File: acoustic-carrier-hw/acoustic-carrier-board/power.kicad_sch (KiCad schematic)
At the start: 59 parts, among them IC1 ECP5-BGA256, U6 TLV62569DRL, U7 TLV62569DRL, U8 TLV62569DRL

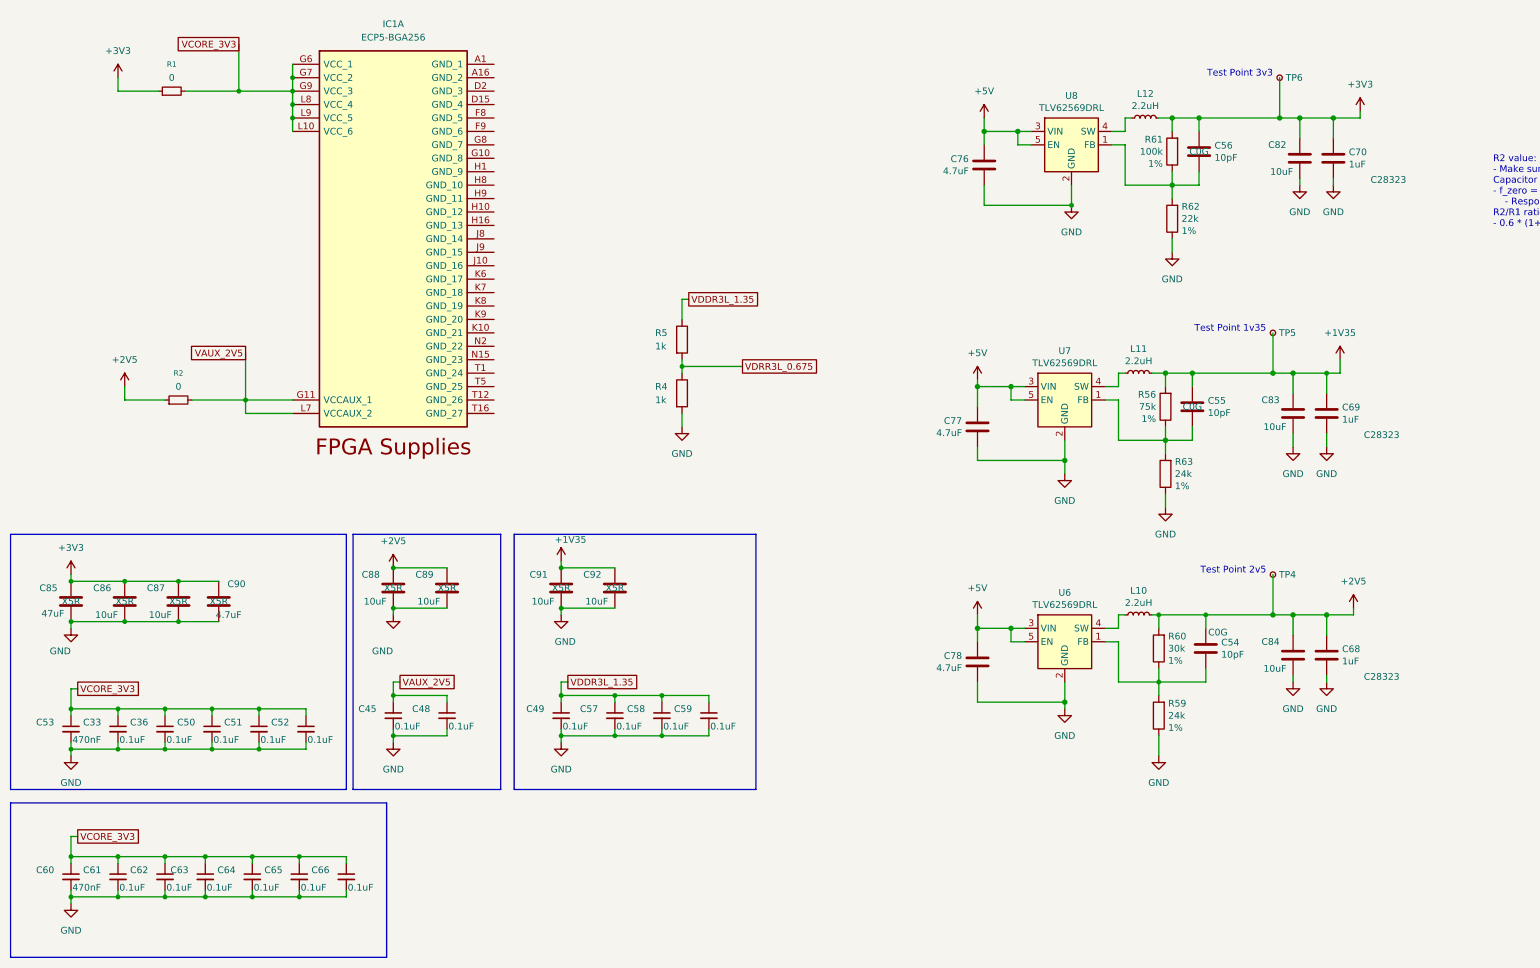
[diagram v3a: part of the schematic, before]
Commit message: [carrier] Added space for ferrite bead in between bulk and decoupling caps
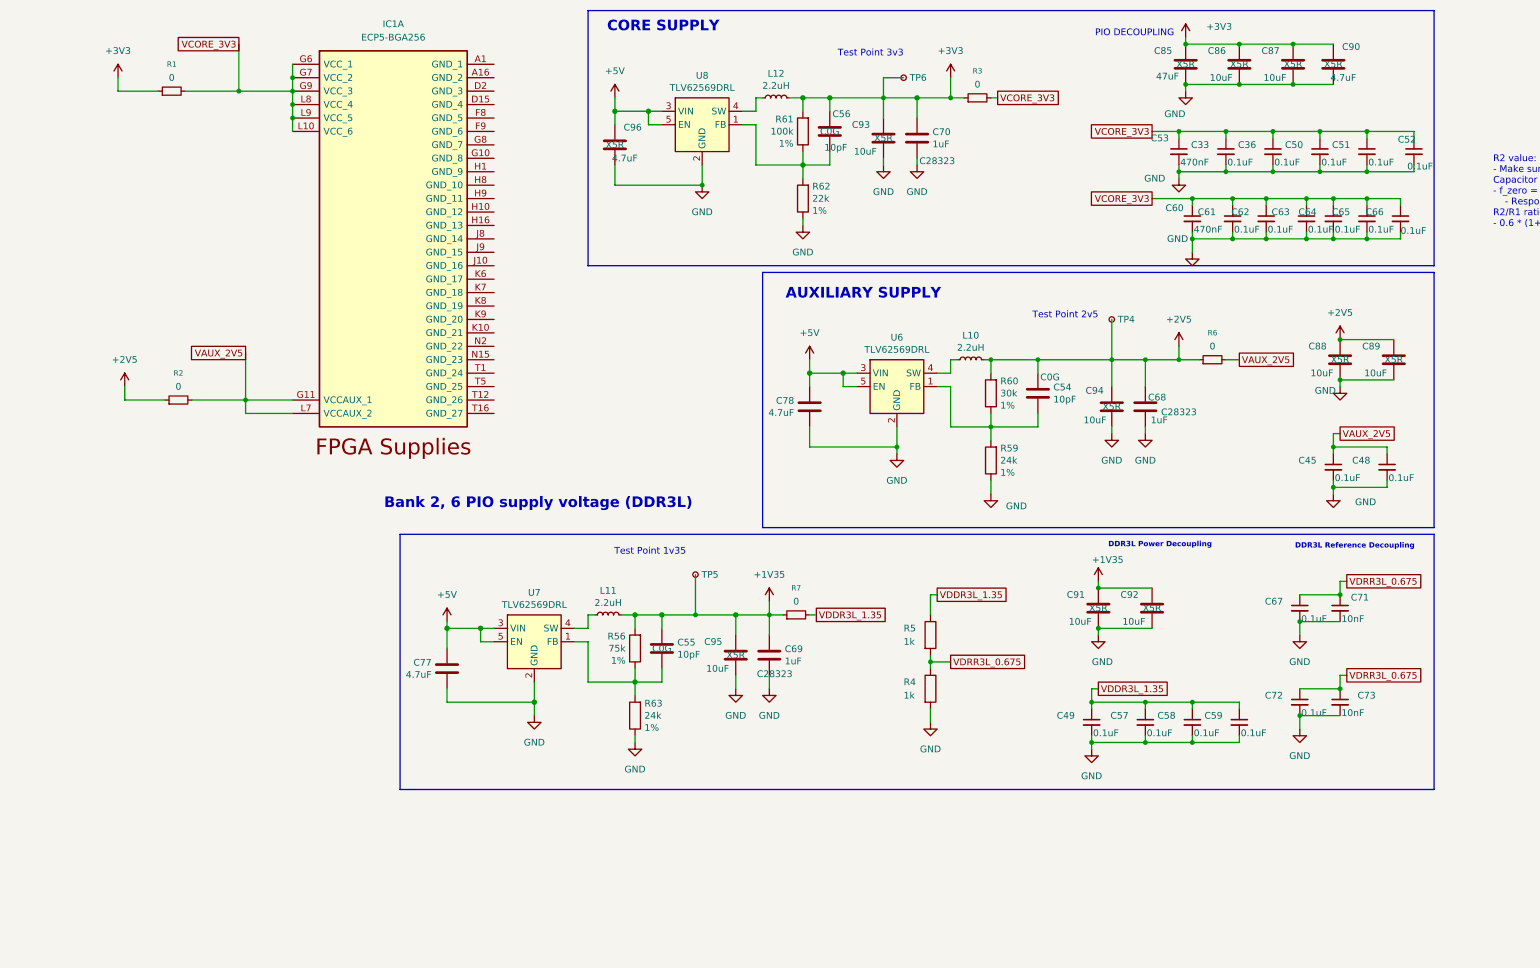
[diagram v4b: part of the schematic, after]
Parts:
- removed C76: 4.7uF, Capacitor_SMD:C_0402_1005Metric, symbol Device:C
- removed C82, C83, C84: 10uF, Capacitor_SMD:C_0603_1608Metric, symbol Device:C
- added C67, C72: 0.1uF, Capacitor_SMD:C_0402_1005Metric, symbol Device:C_Small
- added C71, C73: 10nF, Capacitor_SMD:C_0402_1005Metric, symbol Device:C_Small
- added C93, C94, C95: 10uF, Capacitor_SMD:C_0603_1608Metric, symbol Device:C
- added C96: 4.7uF, Capacitor_SMD:C_0402_1005Metric, symbol Device:C
- added R3, R6, R7: 0, Resistor_SMD:R_0805_2012Metric_Pad1.20x1.40mm_HandSolder, symbol Device:R_Small
- TP6: footprint TestPoint:TestPoint_Pad_D1.5mm -> (none); LPN (none) -> DNP; PN DNP -> (none)
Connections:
- net +1V35: now also C95.1, R7.1
- net +2V5: now also C94.1, R6.1
- net +3V3: now also C93.1, R3.1
- net +5V: now also C96.1
- net GND: now also C67.2, C71.2, C72.2, C73.2, C93.2, C94.2, C95.2, C96.2
- net VAUX_2V5: now also R6.2
- net VCORE_3V3: now also R3.2
- net VDDR3L_1.35: now also R7.2
- net VDRR3L_0.675: now also C67.1, C71.1, C72.1, C73.1
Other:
- note added: "AUXILIARY SUPPLY"
- note added: "Bank 2, 6 PIO supply voltage (DDR3L)"
- note added: "CORE SUPPLY"
- note added: "DDR3L Power Decoupling"
- note added: "DDR3L Reference Decoupling"
- note added: "PIO DECOUPLING"
- moved on the sheet: C33, C36, C45, C48, C49, C50, C51, C52, C53, C54, C55, C56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

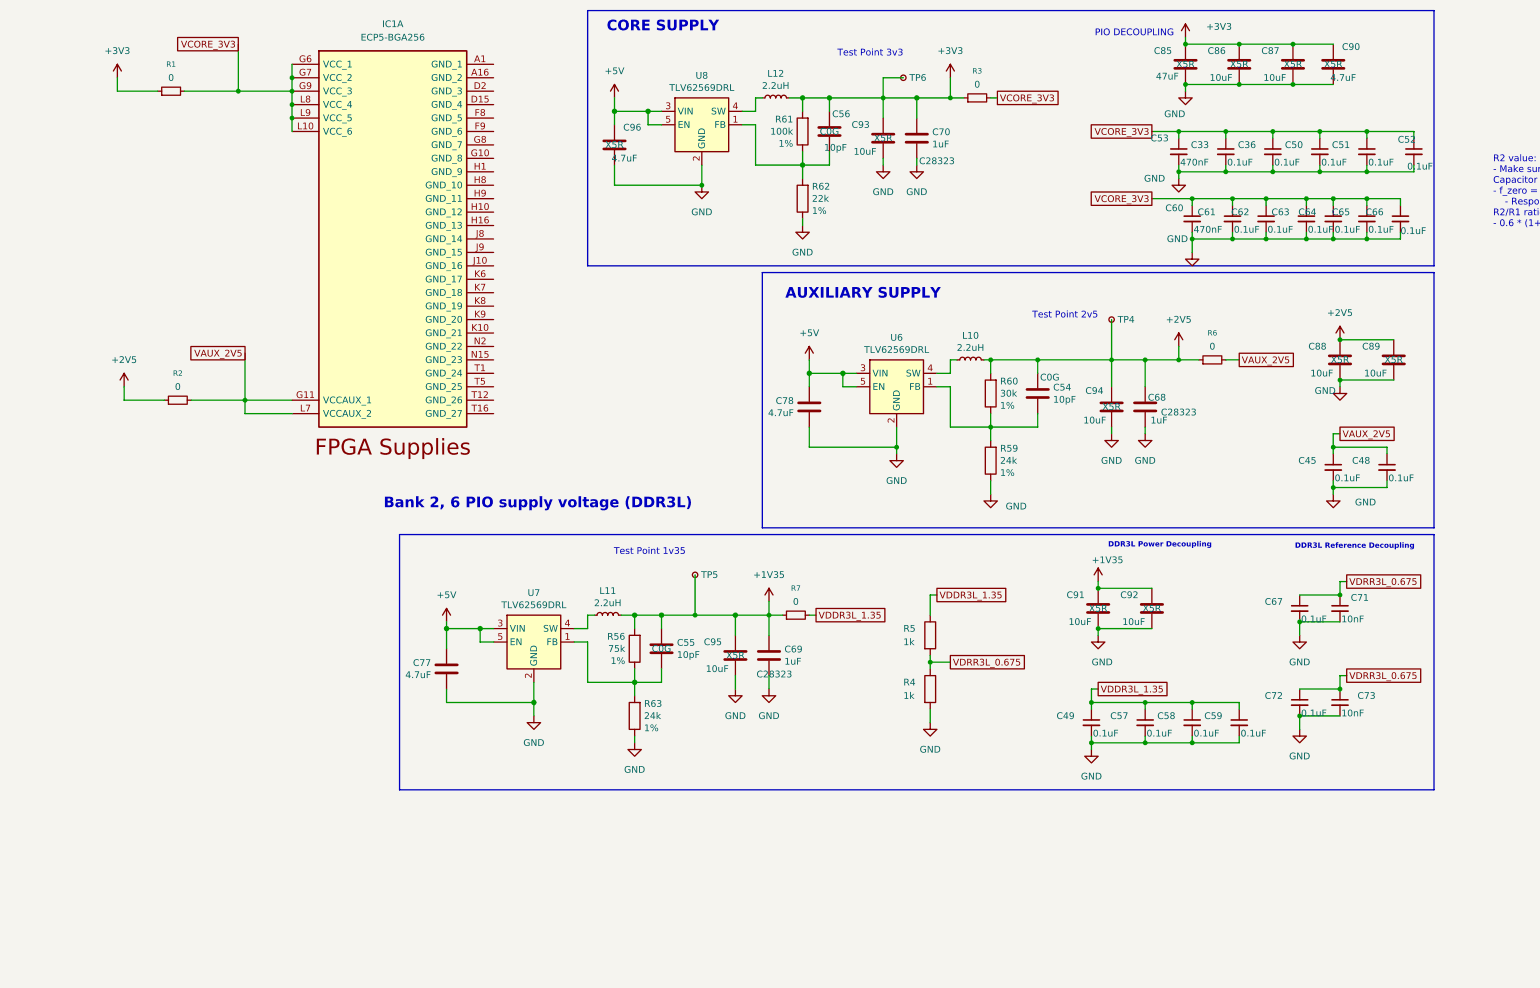
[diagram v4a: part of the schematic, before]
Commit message: [carrier] Added decoupling to ethernet PHY
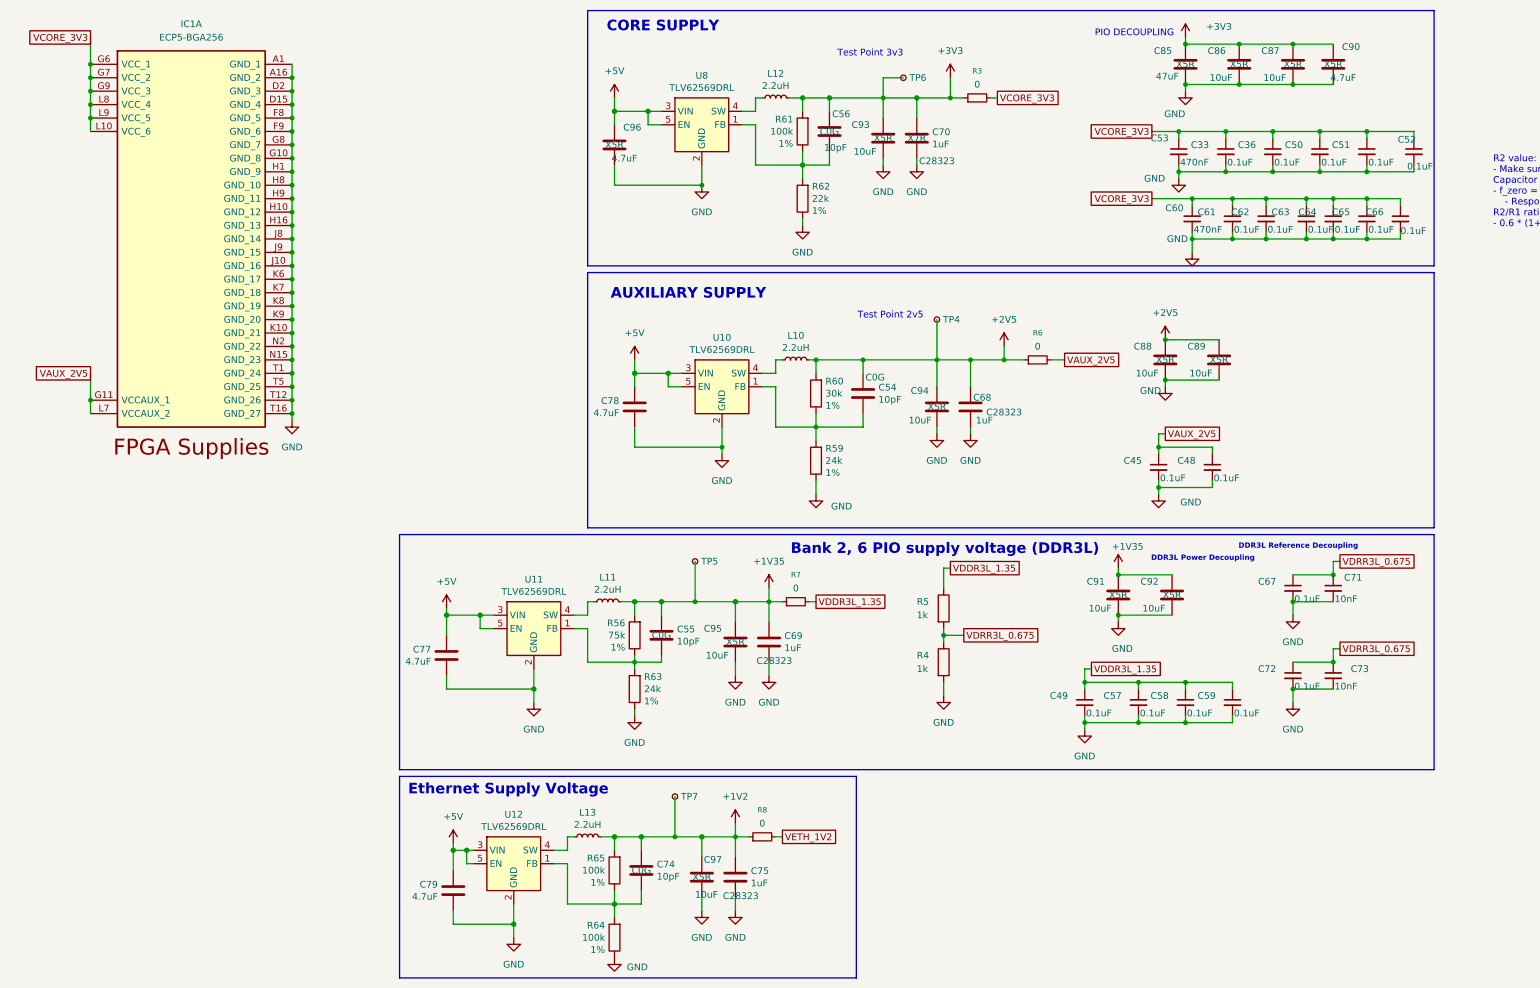
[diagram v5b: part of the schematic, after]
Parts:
- removed R1, R2: 0, Resistor_SMD:R_0805_2012Metric_Pad1.20x1.40mm_HandSolder, symbol Device:R_Small
- removed U6, U7: TLV62569DRL, Package_TO_SOT_SMD:SOT-563, symbol Regulator_Switching:TLV62569DRL
- added C74: 10pF, Capacitor_SMD:C_0402_1005Metric, symbol Device:C
- added C75: 1uF, Capacitor_SMD:C_0805_2012Metric, symbol Device:C
- added C79: 4.7uF, Capacitor_SMD:C_0402_1005Metric, symbol Device:C
- added C97: 10uF, Capacitor_SMD:C_0603_1608Metric, symbol Device:C
- added L13: 2.2uH, Inductor_SMD:L_0805_2012Metric, symbol Device:L_Small
- added R64, R65: 100k, Resistor_SMD:R_0402_1005Metric, symbol Device:R
- added R8: 0, Resistor_SMD:R_0805_2012Metric_Pad1.20x1.40mm_HandSolder, symbol Device:R_Small
- added TP7: TestPoint_Small, TestPoint:TestPoint_Pad_D1.5mm, symbol Connector:TestPoint_Small
- added U10, U11, U12: TLV62569DRL, Package_TO_SOT_SMD:SOT-23-5, symbol Regulator_Switching:TLV62569DRL
- IC1: footprint (none) -> BGA256C80P16X16_1400X1400X170
- U8: footprint Package_TO_SOT_SMD:SOT-563 -> Package_TO_SOT_SMD:SOT-23-5; LPN (none) -> C141836; MPN (none) -> TLV62569DRLR; PN TLV62569DRLR -> (none)
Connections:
- net +5V: now also C79.1, U10.3 (VIN), U10.5 (EN), U11.3 (VIN), U11.5 (EN), U12.3 (VIN), U12.5 (EN)
- net GND: now also IC1.A1 (GND_1), IC1.A16 (GND_2), IC1.D15 (GND_4), IC1.D2 (GND_3), IC1.F8 (GND_5), IC1.F9 (GND_6), IC1.G10 (GND_8), IC1.G8 (GND_7), IC1.H1 (GND_9), IC1.H10 (GND_12), IC1.H16 (GND_13), IC1.H8 (GND_10), IC1.H9 (GND_11), IC1.J10 (GND_16), IC1.J8 (GND_14), IC1.J9 (GND_15), IC1.K10 (GND_21), IC1.K6 (GND_17), IC1.K7 (GND_18), IC1.K8 (GND_19), IC1.K9 (GND_20), IC1.N15 (GND_23), IC1.N2 (GND_22), IC1.T1 (GND_24), IC1.T12 (GND_26), IC1.T16 (GND_27), IC1.T5 (GND_25), C75.2, C79.2, C97.2, R64.1, U10.2 (GND), U11.2 (GND), U12.2 (GND)
- net at C54.2, R59.2, R60.1: now also U10.1 (FB)
- net at C55.2, R56.1, R63.2: now also U11.1 (FB)
- net at L10.1: now also U10.4 (SW)
- net at L11.1: now also U11.4 (SW)
- new net: L13.1, U12.4 (SW)
- new net: C74.2, R64.2, R65.1, U12.1 (FB)
- new net +1V2: C74.1, C75.1, C97.1, L13.2, R65.2, R8.1, TP7.1
- new net VETH_1V2: R8.2
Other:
- note added: "Ethernet Supply Voltage"
- note removed: "Test Point 1v35"
- moved on the sheet: C45, C48, C49, C54, C55, C57, C58, C59, C67, C68, C69, C71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

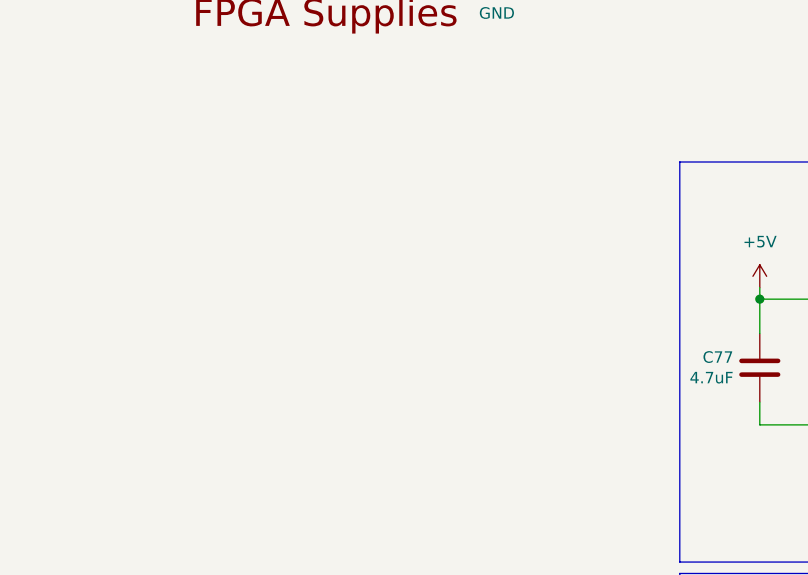
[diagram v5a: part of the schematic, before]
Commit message: [carrier] Added usb power + communication circuitry (next) Connect ADC pins to bank 0, select PWM pins, check connectors for power board
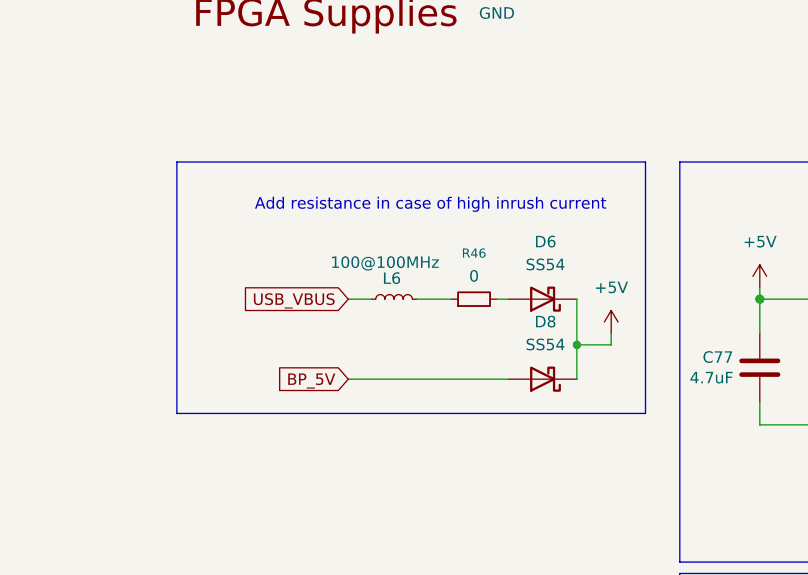
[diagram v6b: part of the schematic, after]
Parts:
- added D6, D8: SS54, Diode_SMD:D_SMA-SMB_Universal_Handsoldering, symbol Device:D_Schottky
- added L6: 100@100MHz, Inductor_SMD:L_0805_2012Metric, symbol Device:L_Small
- added R46: 0, Resistor_SMD:R_0805_2012Metric_Pad1.20x1.40mm_HandSolder, symbol Device:R_Small
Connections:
- net +5V: now also D6.1 (K), D8.1 (K)
- new net: L6.1, R46.1
- new net: D6.2 (A), R46.2
- new net BP_5V: D8.2 (A)
- new net USB_VBUS: L6.2
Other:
- note added: "Add resistance in case of high inrush current"

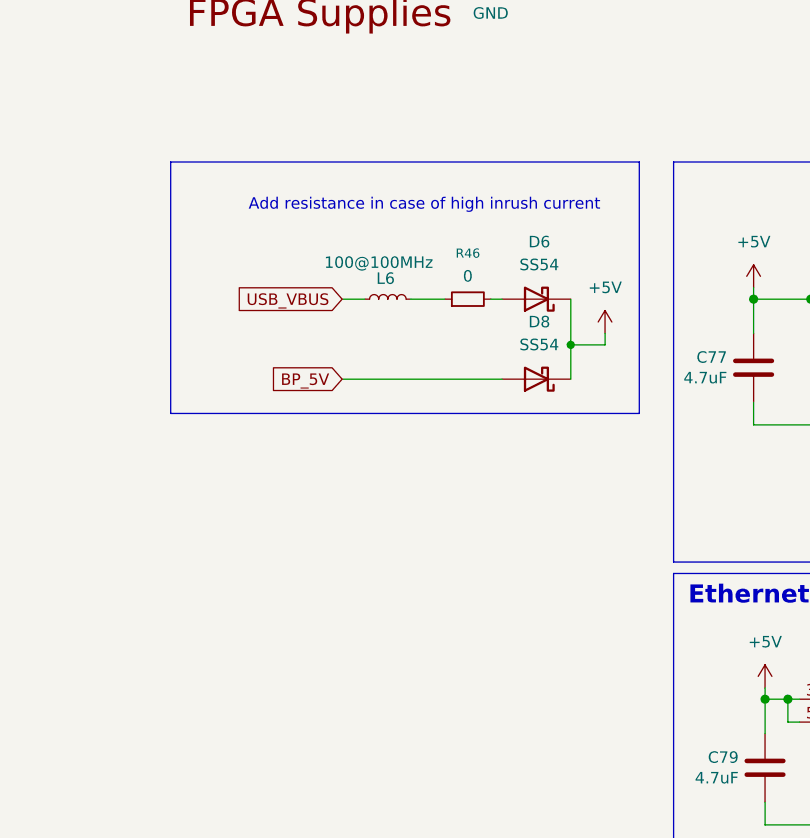
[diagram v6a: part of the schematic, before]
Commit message: [carrier] Added adc connections and PWM + poweer connectors
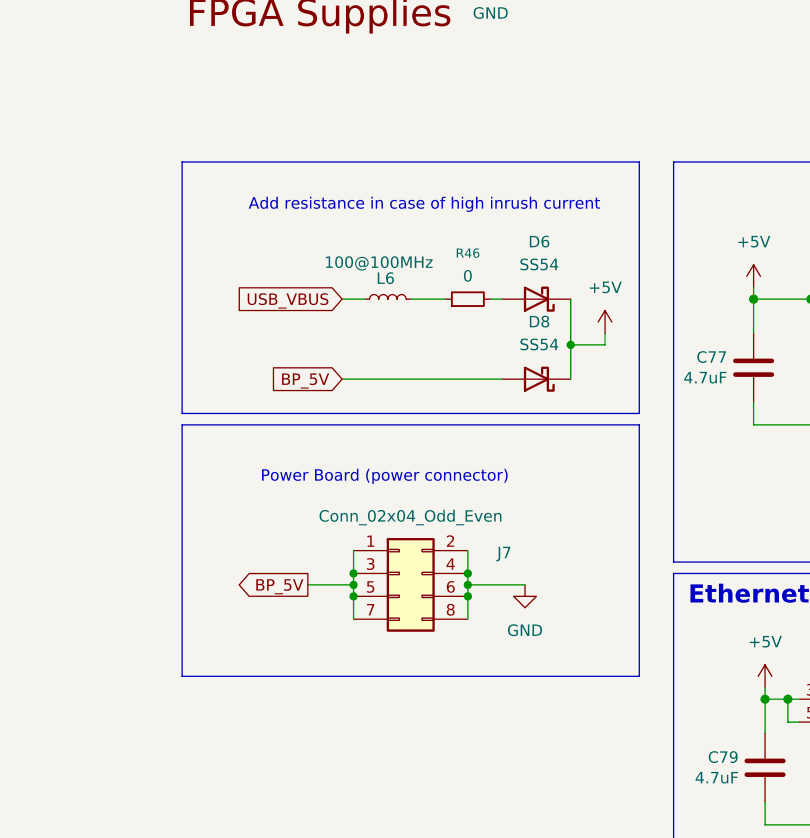
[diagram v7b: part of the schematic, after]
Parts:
- added J7: Conn_02x04_Odd_Even, Connector_PinSocket_2.54mm:PinSocket_2x04_P2.54mm_Horizontal, symbol Connector_Generic:Conn_02x04_Odd_Even
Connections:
- net BP_5V: now also J7.1 (Pin_1), J7.3 (Pin_3), J7.5 (Pin_5), J7.7 (Pin_7)
- net GND: now also J7.2 (Pin_2), J7.4 (Pin_4), J7.6 (Pin_6), J7.8 (Pin_8)
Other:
- note added: "Power Board (power connector)"
